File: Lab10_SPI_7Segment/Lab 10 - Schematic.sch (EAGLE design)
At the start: 6 parts, among them U1 328P, U2 328P

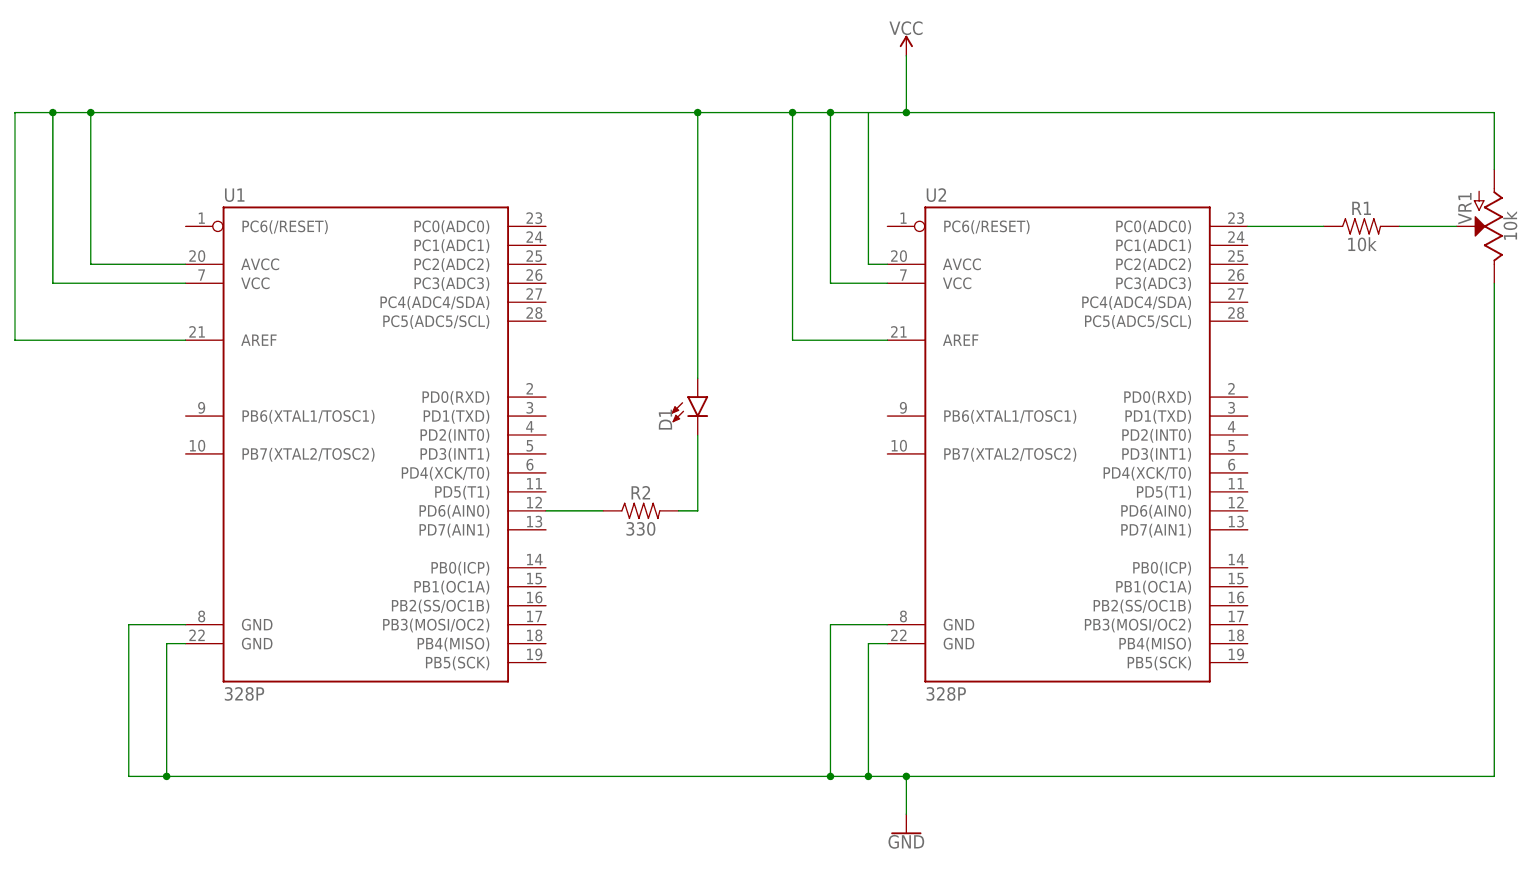
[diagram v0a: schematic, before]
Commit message: adding lab 10 schematic and removing temporary copies
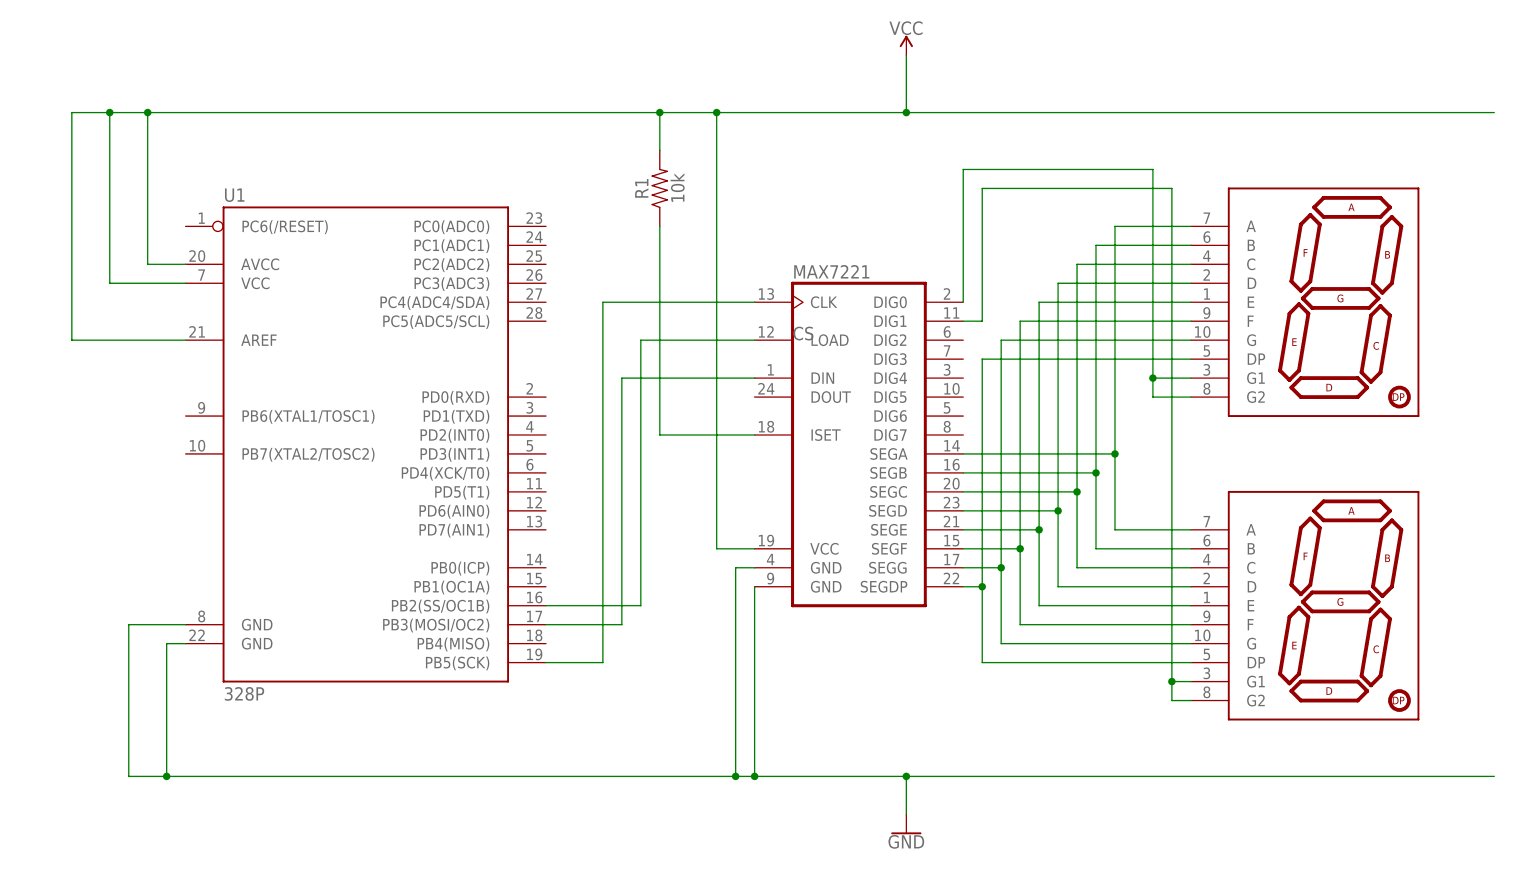
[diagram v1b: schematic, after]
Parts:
- removed D1: (no value), SparkFun-LED:LED3MM
- removed R2: 330, SparkFun-Resistors:330OHM-HORIZ-1/10W-5%
- removed U2: 328P, SparkFun-IC-Microcontroller:ATMEGA328P_PDIP
- removed VR1: 10k, SparkFun-Resistors:POTENTIOMETER-PTH-9MM-1/20W-20%-KIT
- added MAX7221: MAX7219CNG, maxim:MAX7219CNG
- added U$1, U$2: YSD-160AB3C-8, SparkFun-LED:7-SEGMENT-1DIGIT-1INCH-BLUE
- R1: device SparkFun-Resistors:10KOHM-HORIZ-1/4W-5% -> SparkFun-Resistors:10KOHM-HORIZ-1/4W-1%
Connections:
- removed net N$4: D1.C, R2.2
- new net CS: MAX7221.LOAD, U1.PB2(SS/OC1B)
- new net N$10: MAX7221.SEGE, U$1.E, U$2.E
- new net N$11: MAX7221.SEGD, U$1.D, U$2.D
- new net N$12: MAX7221.SEGA, U$1.A, U$2.A
- new net N$13: MAX7221.DIG0, U$1.G1, U$1.G2
- new net N$14: MAX7221.DIG1, U$2.G1, U$2.G2
- new net N$5: MAX7221.SEGB, U$1.B, U$2.B
- new net N$6: MAX7221.ISET, R1.1
- new net N$7: MAX7221.SEGDP, U$1.DP, U$2.DP
- new net N$8: MAX7221.SEGG, U$1.G, U$2.G
- new net N$9: MAX7221.SEGF, U$1.F, U$2.F
- net GND: now also MAX7221.GND@1, MAX7221.GND@2; no longer U2.GND@1, U2.GND@2, VR1.E
- net N$1: now also MAX7221.SEGC, U$1.C, U$2.C; no longer R1.2, VR1.S
- net N$2: now also MAX7221.CLK, U1.PB5(SCK); no longer R1.1, U2.PC0(ADC0)
- net N$3: now also MAX7221.DIN, U1.PB3(MOSI/OC2); no longer R2.1, U1.PD6(AIN0)
- net VCC: now also MAX7221.VCC, R1.2; no longer D1.A, U2.AREF, U2.AVCC, U2.VCC, VR1.A
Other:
- moved on the sheet: R1
